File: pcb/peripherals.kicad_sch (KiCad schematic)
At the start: 0 parts

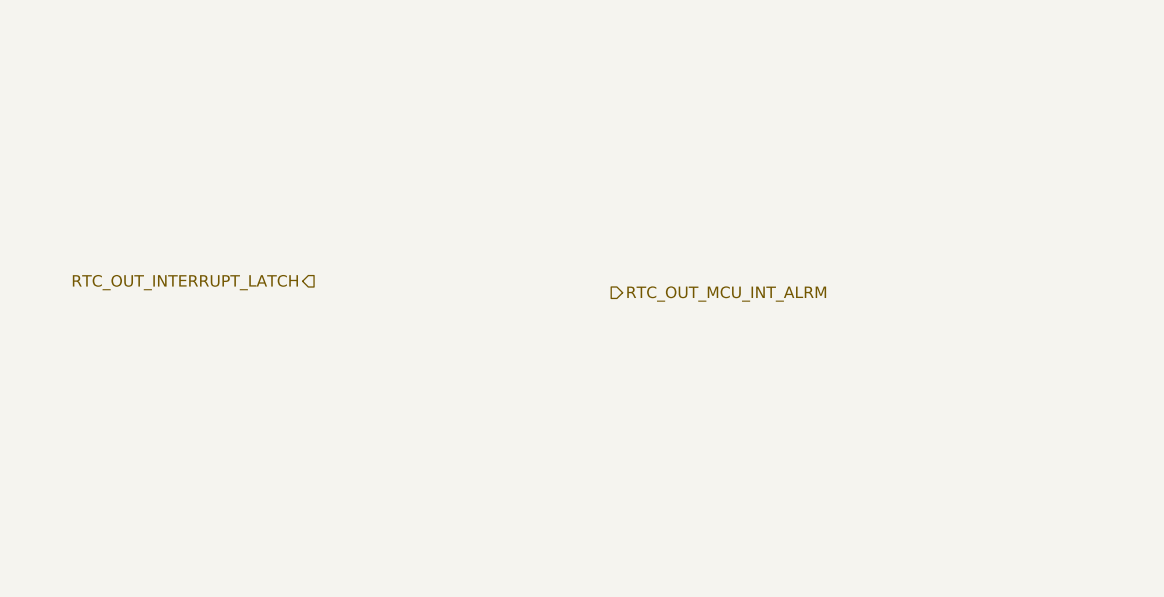
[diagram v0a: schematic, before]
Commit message: Build out PCF8563 RTC peripheral circuit and wire into VRAW latch/MCU
- U14 (PCF8563T) with NDK 9pF crystal (Y2) and DNP OSCI trim cap (C43)
- Coin-cell backup diode-OR: D2/D3 (BAS116) commoned into VDD, BT3
  (CR2032) as backup source, main 3.3V rail as primary
- INT -> Q8 (AO3407A, 3.3V-domain inverter) -> Q7 (BSS138, voltage-safe
  level shift) -> RTC_OUT_INTERRUPT_LATCH, with R31 gate pull-down so
  Q7 has a defined off-state; preserves active-low assert sense onto
  the shared VRAW latch wake node
- R32/R33 (10k) I2C pull-ups on the shared SDA/SCL bus (mcu-esp32,
  Peripherals, and the fuel gauge on Power all share one bus/pull-up
  pair)
- Bump kicad_gx_library for the vendored BAS116LT1G symbol/footprint

Co-Authored-By: Claude Sonnet 5 <noreply@anthropic.com>
Claude-Session: https://claude.ai/code/session_01LhLkuH6sQ5GbUZ61bG7p2h
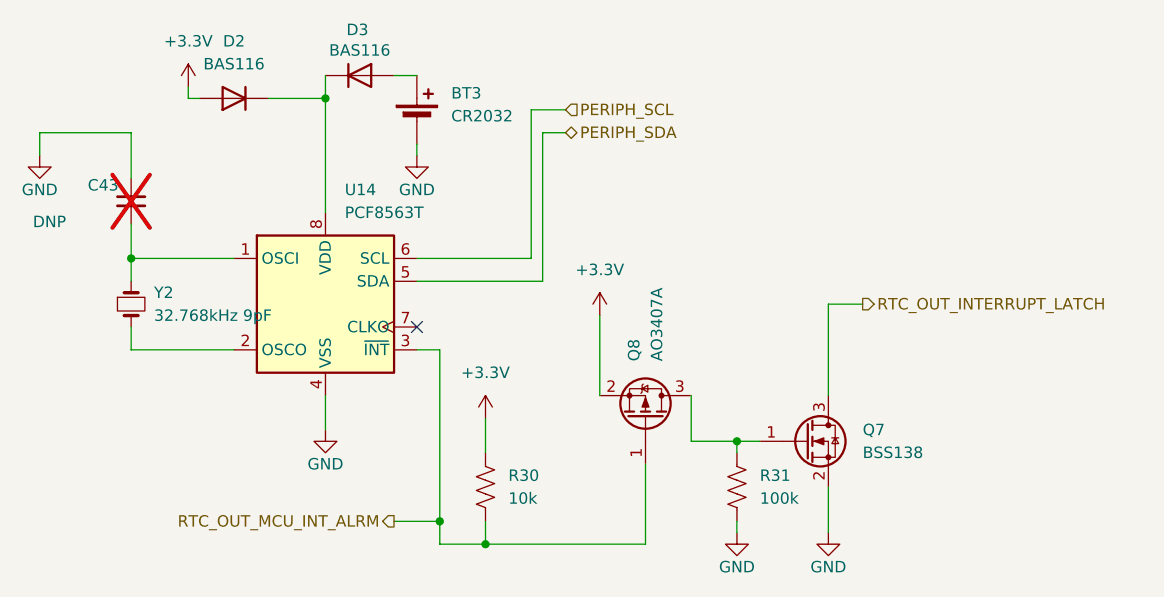
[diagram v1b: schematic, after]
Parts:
- added BT3: CR2032, Battery:Battery_Panasonic_CR2032-HFN_Horizontal_CircularHoles, symbol Device:Battery_Cell
- added C43: DNP, Capacitor_SMD:C_0603_1608Metric, symbol Device:C_Small
- added D2, D3: BAS116, Package_TO_SOT_SMD:TSOT-23, symbol Diode:BAS16W
- added Q7: BSS138, Package_TO_SOT_SMD:SOT-23, symbol Transistor_FET:BSS138
- added Q8: AO3407A, Package_TO_SOT_SMD:SOT-23, symbol Transistor_FET:AO3401A
- added R30: 10k, Resistor_SMD:R_0603_1608Metric, symbol Device:R_US
- added R31: 100k, Resistor_SMD:R_0603_1608Metric, symbol Device:R_US
- added U14: PCF8563T, Package_SO:SOIC-8_3.9x4.9mm_P1.27mm, symbol Timer_RTC:PCF8563T
- added Y2: 32.768kHz 9pF, Crystal:Crystal_SMD_3215-2Pin_3.2x1.5mm, symbol PCM_SparkFun-Clock:Crystal
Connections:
- net RTC_OUT_INTERRUPT_LATCH: now also Q7.3 (D)
- net RTC_OUT_MCU_INT_ALRM: now also Q8.1 (G), R30.1, U14.3 (~{INT})
- new net: C43.2, U14.1 (OSCI), Y2.1
- new net: U14.2 (OSCO), Y2.2
- new net: Q7.1 (G), Q8.3 (D), R31.2
- new net: BT3.1 (+), D3.1 (A)
- new net: D2.3 (K), D3.3 (K), U14.8 (VDD)
- new net +3.3V: D2.1 (A), Q8.2 (S), R30.2
- new net GND: BT3.2 (-), C43.1, Q7.2 (S), R31.1, U14.4 (VSS)
- new net PERIPH_SCL: U14.6 (SCL)
- new net PERIPH_SDA: U14.5 (SDA)
- no-connect marks 0 -> 1

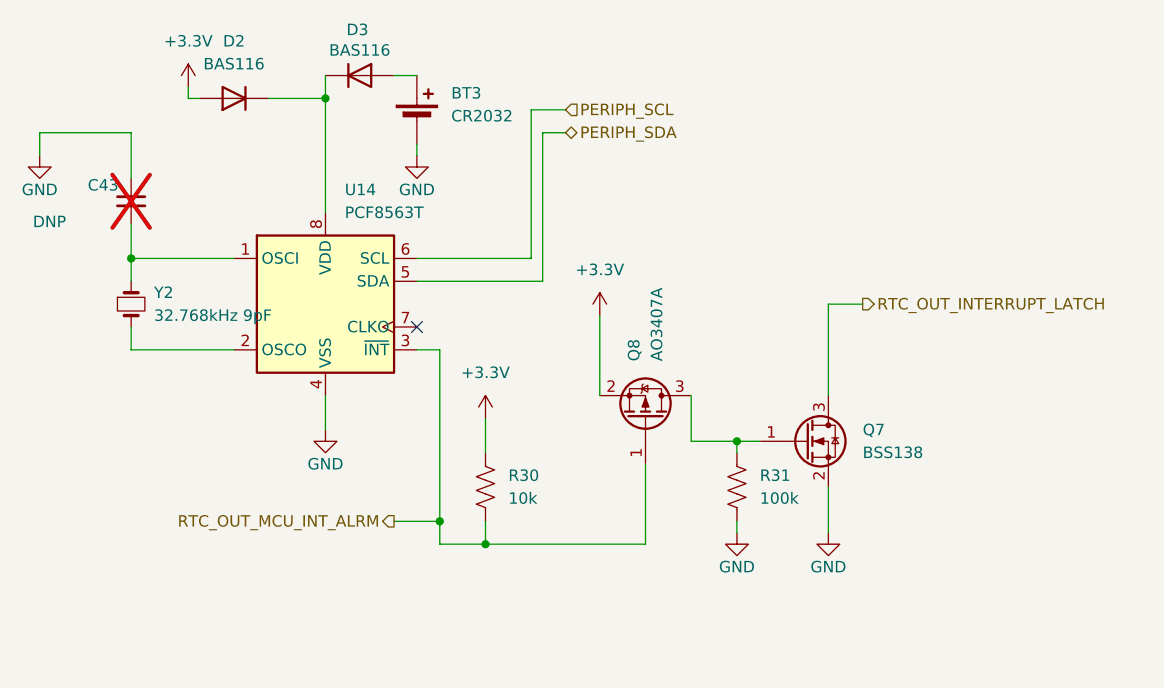
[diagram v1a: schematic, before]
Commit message: Add IC inventory doc; RTC VDD bypass cap, CR2032 holder, SD holder note
- New _docs/ic_inventory.md: every IC/module placed or planned, LCSC
  MPN/price/stock/brand for each, real parts chosen for not-yet-placed
  items per stated price/stock/brand-reputation preference
- peripherals.kicad_sch: VDD/VSS bypass cap (C44) on U14, and the
  physical CR2032 holder footprint in place of the bare cell symbol
- controller_platform.md: record the Molex 472192001 (LCSC C164170)
  flip-top microSD holder choice
- Bump kicad_gx_library for the battery holder and microSD socket parts

Co-Authored-By: Claude Sonnet 5 <noreply@anthropic.com>
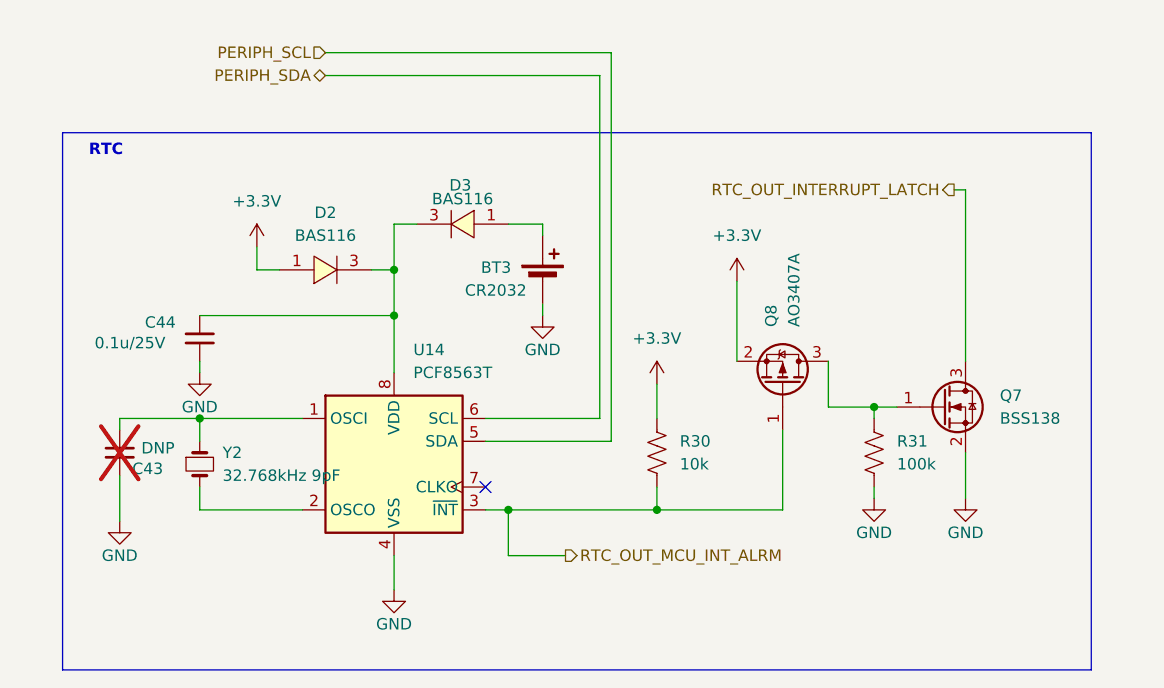
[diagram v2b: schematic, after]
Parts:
- added C44: 0.1u/25V, Capacitor_SMD:C_0603_1608Metric, symbol Device:C_Small
- D2, D3: symbol Diode:BAS16W -> kicad_gx_library:BAS116LT1G
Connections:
- net GND: now also C44.2
- net PERIPH_SCL: now also U14.5 (SDA); no longer U14.6 (SCL)
- net PERIPH_SDA: now also U14.6 (SCL); no longer U14.5 (SDA)
- net at D2.3, D3.3, U14.8 (VDD): now also C44.1
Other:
- note added: "RTC"
- moved on the sheet: BT3, C43, Q7, Q8, R30, R31, U14, Y2

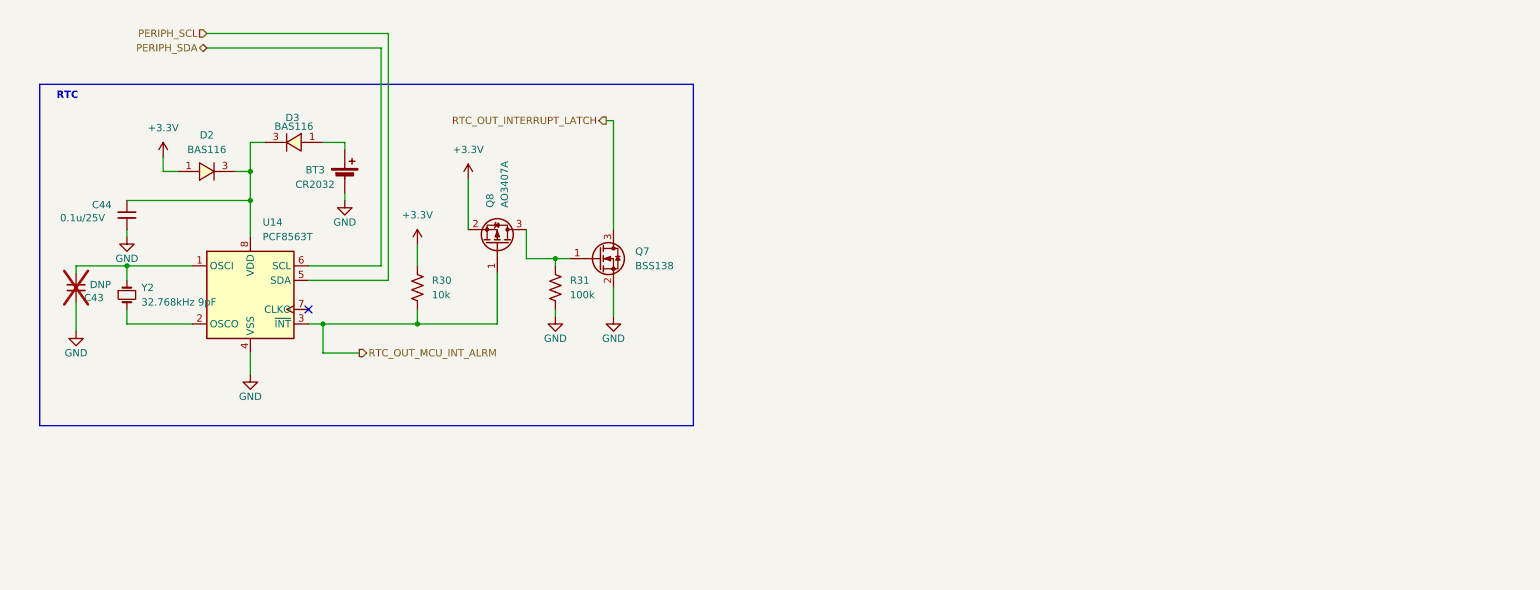
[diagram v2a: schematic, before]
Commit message: Wire up PCA9555 expansion IO section, source LEDs/resistors, swap 3.3V LDO to LM1117
- PCA9555PW expansion IO: DIP switch (SW4, IO0_0-3), onboard buttons
  (SW7-10), status LEDs (D7-10) with sourced series resistors, external
  JST breakouts (J4-7/R39-42) for IO0_4-7, INT pull-up (R34), VDD bypass
  (C49), address pins grounded (addr 0x20)
- Route PCA9555 INT (PERIPH_IO_INT) across the Power/mcu-esp32 top-level
  sheets to the ESP32-S3 (MCU_IN_IO_INT)
- Source real YAGEO MPN/LCSC part numbers for R30/R31/R34-R42
- Fix D10 LED (was orange 0603 with an LCSC part# that resolved to a
  different, wrong part) -> yellow 0805 APTD2012LSYCK, verified Vf/LCSC
  match, matching D7-9's package family
- Fix stale copy-pasted Datasheet links on D7-9 and R31/R35
- Swap 3.3V LDO from AMS1117-3.3 to TI LM1117IMPX-3.3/NOPB (5V LDO swap
  from LM1085IS-5.0 still pending)

Co-Authored-By: Claude Sonnet 5 <noreply@anthropic.com>
Claude-Session: https://claude.ai/code/session_01LhLkuH6sQ5GbUZ61bG7p2h
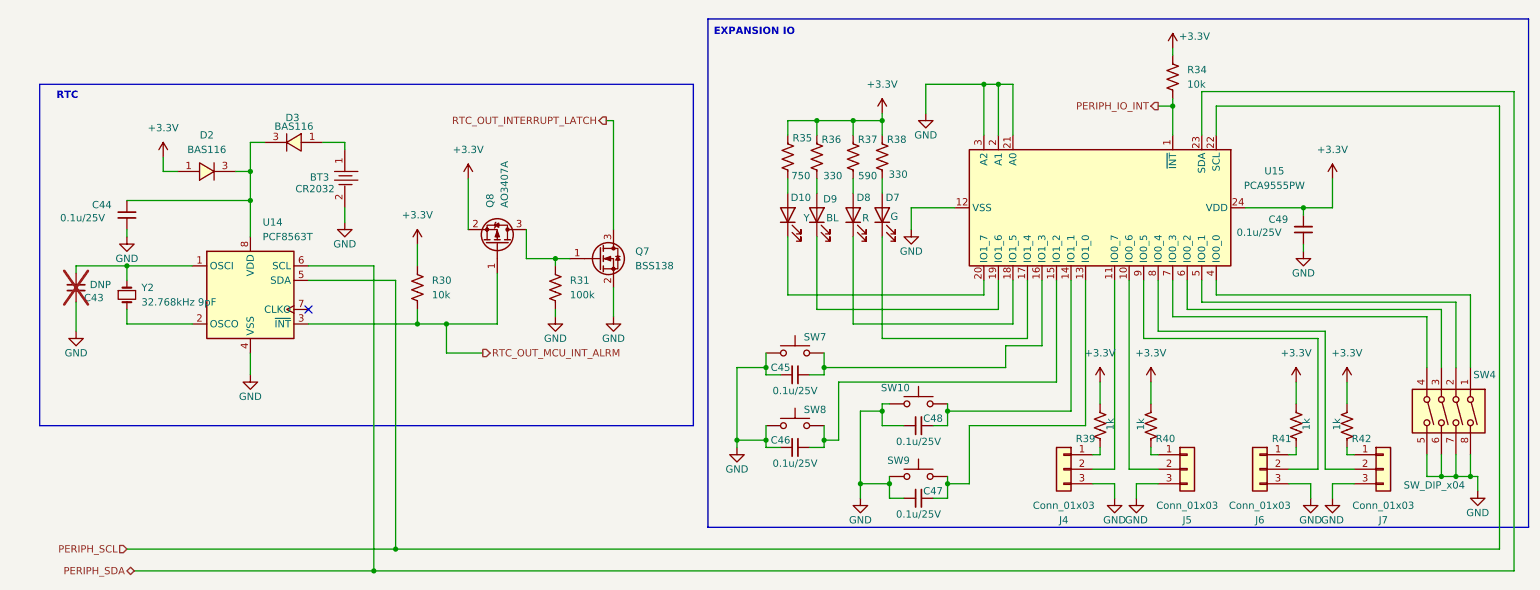
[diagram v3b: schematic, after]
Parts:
- added C45, C46, C47, C48, C49: 0.1u/25V, Capacitor_SMD:C_0603_1608Metric, symbol Device:C_Small
- added D10: Y, LED_SMD:LED_0805_2012Metric, symbol Device:LED
- added D7: G, LED_SMD:LED_0805_2012Metric, symbol Device:LED
- added D8: R, LED_SMD:LED_0805_2012Metric, symbol Device:LED
- added D9: BL, LED_SMD:LED_0805_2012Metric, symbol Device:LED
- added J4, J5, J6, J7: Conn_01x03, Connector_JST:JST_PH_B3B-PH-SM4-TB_1x03-1MP_P2.00mm_Vertical, symbol Connector_Generic:Conn_01x03
- added R34: 10k, Resistor_SMD:R_0603_1608Metric, symbol Device:R_US
- added R35: 750, Resistor_SMD:R_0603_1608Metric, symbol Device:R_US
- added R36, R38: 330, Resistor_SMD:R_0603_1608Metric, symbol Device:R_US
- added R37: 590, Resistor_SMD:R_0603_1608Metric, symbol Device:R_US
- added R39, R40, R41, R42: 1k, Resistor_SMD:R_0603_1608Metric, symbol Device:R_US
- added SW10, SW7, SW8, SW9: GENERAL, Button_Switch_SMD:SW_SPST_PTS645Sx43SMTR92, symbol Switch:SW_Push
- added SW4: SW_DIP_x04, Button_Switch_SMD:SW_DIP_SPSTx04_Slide_KingTek_DSHP04TS_W7.62mm_P1.27mm, symbol Switch:SW_DIP_x04
- added U15: PCA9555PW, Package_SO:TSSOP-24_4.4x7.8mm_P0.65mm, symbol Interface_Expansion:PCA9555PW
- BT3: footprint Battery:Battery_Panasonic_CR2032-HFN_Horizontal_CircularHoles -> kicad_gx_library:BAT-SMD_BS-08-B2AA016; symbol Device:Battery_Cell -> kicad_gx_library:BS-08-B2AA020-R; Imported (none) -> 2026-09-20; LCSC Part (none) -> C964787; MPN (none) -> BS-08-B2AA020-R; Manufacturer (none) -> MYOUNG(美阳); Source (none) -> easyeda2kicad
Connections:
- net +3.3V: now also C49.1, R34.2, R35.1, R36.2, R37.1, R38.1, R39.1, R40.1, R41.1, R42.1, U15.24 (VDD)
- net GND: now also C45.1, C46.1, C47.2, C48.2, C49.2, J4.3 (Pin_3), J5.3 (Pin_3), J6.3 (Pin_3), J7.3 (Pin_3), SW10.1, SW4.5, SW4.6, SW4.7, SW4.8, SW7.2, SW8.2, SW9.1, U15.12 (VSS), U15.2 (A1), U15.21 (A0), U15.3 (A2)
- net PERIPH_SCL: now also U15.22 (SCL)
- net PERIPH_SDA: now also U15.23 (SDA)
- new net: C47.1, SW9.2, U15.13 (IO1_0)
- new net: D8.1 (K), U15.18 (IO1_5)
- new net: D8.2 (A), R37.2
- new net: SW4.1, U15.4 (IO0_0)
- new net: SW4.2, U15.5 (IO0_1)
- new net: SW4.3, U15.6 (IO0_2)
- new net: SW4.4, U15.7 (IO0_3)
- new net: J6.1 (Pin_1), R41.2
- new net: C46.2, SW8.1, U15.15 (IO1_2)
- new net: J6.2 (Pin_2), U15.9 (IO0_5)
- new net: J4.1 (Pin_1), R39.2
- new net: J7.1 (Pin_1), R42.2
- new net: J7.2 (Pin_2), U15.8 (IO0_4)
- new net: D9.2 (A), R36.1
- new net: D7.1 (K), U15.17 (IO1_4)
- new net: D7.2 (A), R38.2
- new net: J5.1 (Pin_1), R40.2
- new net: J5.2 (Pin_2), U15.10 (IO0_6)
- new net: D10.2 (A), R35.2
- new net: J4.2 (Pin_2), U15.11 (IO0_7)
- new net: C48.1, SW10.2, U15.14 (IO1_1)
- new net: C45.2, SW7.1, U15.16 (IO1_3)
- new net: D9.1 (K), U15.19 (IO1_6)
- new net: D10.1 (K), U15.20 (IO1_7)
- new net PERIPH_IO_INT: R34.1, U15.1 (~{INT})
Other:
- note added: "EXPANSION IO"

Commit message: Fix DRC/ERC issues: PWR_FLAG on USB-C UART VBUS net, BAS116 NC pin resync
- Add PWR_FLAG to the unpowered net on usbc-programming-uart.kicad_sch
  to resolve an ERC power-pin-not-driven error
- Re-sync D2/D3 (BAS116LT1G) in peripherals.kicad_sch from the library
  to pick up the corrected pin 2 electrical type

Co-Authored-By: Claude Sonnet 5 <noreply@anthropic.com>
Claude-Session: https://claude.ai/code/session_01LhLkuH6sQ5GbUZ61bG7p2h
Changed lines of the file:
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@@
 	)
 	(junction
+		(at 58.42 35.56)
+		(diameter 0)
+		(color 0 0 0 0)
+	)
+	(junction
 		(at 186.69 25.4)
 		(diameter 0)
@@
 					(unit 1)
 				)
+			)
+		)
+	)
+	(symbol
+		(lib_id "power:PWR_FLAG")
+		(at 58.42 35.56 0)
+		(unit 1)
+		(body_style 1)
+		(exclude_from_sim no)
+		(in_bom yes)
+		(on_board yes)
+		(in_pos_files yes)
+		(dnp no)
+		(fields_autoplaced yes)
+		(property "Reference" "#FLG020"
+			(at 58.42 33.655 0)
+			(hide yes)
+			(show_name no)
+			(do_not_autoplace no)
+			(effects
+				(font
+					(size 1.27 1.27)
+				)
+			)
+		)
+		(property "Value" "PWR_FLAG"
+			(at 58.42 30.48 0)
+			(show_name no)
+			(do_not_autoplace no)
+			(effects
+				(font
+					(size 1.27 1.27)
+				)
+			)
+		)
+		(property "Footprint" ""
+			(at 58.42 35.56 0)
+			(hide yes)
+			(show_name no)
+			(do_not_autoplace no)
+			(effects
+				(font
+					(size 1.27 1.27)
+				)
+			)
+		)
+		(property "Datasheet" ""
+			(at 58.42 35.56 0)
+			(hide yes)
+			(show_name no)
+			(do_not_autoplace no)
+			(effects
+				(font
+					(size 1.27 1.27)
+				)
+			)
+		)
+		(property "Description" "Special symbol for telling ERC where power comes from"
+			(at 58.42 35.56 0)
+			(hide yes)
+			(show_name no)
+			(do_not_autoplace no)
+			(effects
+				(font
+					(size 1.27 1.27)
+				)
+			)
+		)
+		(pin "1"
+		)
+		(instances
+			(project "foxhunt1"
+				(path "/8399ba4b-9428-480d-8b65-76cf154b97a5/be75080d-eece-47db-bf9a-20f8f91d5133"
+					(reference "#FLG020")
+					(unit 1)
+				)
